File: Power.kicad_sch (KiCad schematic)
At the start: 0 parts

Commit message: [#81782] Add DC section
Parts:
- added C17: C_1u_25V_0402, antmicro-footprints:C_0402_1005Metric, symbol antmicroCapacitors0402:C_1u_25V_0402
- added C18, C23, C24, C25, C30, C31: C_100n_0402, antmicro-footprints:C_0402_1005Metric, symbol antmicroCapacitors0402:C_100n_0402
- added C19, C20, C21, C22: C_22u_25V_0805, antmicro-footprints:C_0805_2012Metric, symbol antmicroCapacitorsmisc:C_22u_25V_0805
- added C26, C27: C_1u_0402, antmicro-footprints:C_0402_1005Metric, symbol antmicroCapacitors0402:C_1u_0402
- added C28, C29: C_4u7_25V_0402, antmicro-footprints:C_0402_1005Metric, symbol antmicroCapacitors0402:C_4u7_25V_0402
- added C32, C33, C34, C35, C36, C37, C38, C39: C_22u_16V_0603, antmicro-footprints:C_0603_1608Metric_EIA, symbol antmicroCapacitors0603:C_22u_16V_0603
- added D1, D3: DF2S30FS_SOD, antmicro-footprints:SOD-923, symbol antmicroTVSDiodes:DF2S30FS_SOD
- added D2: LED_G_0603_LTST-C190GKT, antmicro-footprints:LED_0603_1608Metric_G, symbol antmicroLEDIndicationDiscrete:LED_G_0603_LTST-C190GKT
- added D4, D5: ESD9X5.0ST5G, antmicro-footprints:SOD-923, symbol antmicroTVSDiodes:ESD9X5.0ST5G
- added J2: Molex_Nano-Fit_1x2_SMD_1054301202, antmicro-footprints:Conn_Molex_Nano-Fit_1x2_SMD_1054301202, symbol antmicroWire2BoardConnectors:Molex_Nano-Fit_1x2_SMD_1054301202
- added L1: L_1u_20A_Bourns-SRP6050CA, antmicro-footprints:L_Bourns-SRP6050CA, symbol antmicroFixedInductors:L_1u_20A_Bourns-SRP6050CA
- added L2: L_560n_17.7A_Bourns-SRP5030CA, antmicro-footprints:L_Bourns-SRP5030CA, symbol antmicroFixedInductors:L_560n_17.7A_Bourns-SRP5030CA
- added Q1, Q3, Q5: SSM3J332R, antmicro-footprints:SOT-23-3, symbol antmicroTransistorsFETsMOSFETsSingle:SSM3J332R
- added Q2: BCM857BS-7-F, antmicro-footprints:SOT-363, symbol antmicroTransistorsBipolarArrays:BCM857BS-7-F
- added Q4: PJE138K, antmicro-footprints:SOT-523, symbol antmicroTransistorsFETsMOSFETsSingle:PJE138K
- added R10, R11, R12, R15, R16, R9: R_499k_0402, antmicro-footprints:R_0402_1005Metric, symbol antmicroResistors0402:R_499k_0402
- added R13: R_20k_0402, antmicro-footprints:R_0402_1005Metric, symbol antmicroResistors0402:R_20k_0402
- added R14: R_2k7_0402, antmicro-footprints:R_0402_1005Metric, symbol antmicroResistors0402:R_2k7_0402
- added R17: R_0R_0402, antmicro-footprints:R_0402_1005Metric, symbol antmicroResistors0402:R_0R_0402
- added R18: R_73k2_0402, antmicro-footprints:R_0402_1005Metric, symbol antmicroResistors0402:R_73k2_0402
- added R19, R21, R24, R3, R4, R8: R_10k_0402, antmicro-footprints:R_0402_1005Metric, symbol antmicroResistors0402:R_10k_0402
- added R20: R_45k3_0402, antmicro-footprints:R_0402_1005Metric, symbol antmicroResistors0402:R_45k3_0402
- added R22, R23, R25, R6: R_0R_22.4A_0603, antmicro-footprints:R_0603_1608Metric, symbol antmicroResistors0603:R_0R_22.4A_0603
- added R5, R7: R_4k7_0402, antmicro-footprints:R_0402_1005Metric, symbol antmicroResistors0402:R_4k7_0402
- added TP1, TP2, TP3, TP4: TP_0.75mm_SMD, antmicro-footprints:TP_SMD_0.75mm, symbol antmicroTestPoints:TP_0.75mm_SMD
- added U1, U2: SIC431AED-T1-GE3, antmicro-footprints:MLP44-24L_4x4x0.75mm, symbol antmicroDCDCConverters:SIC431AED-T1-GE3
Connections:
- new net: D1.1 (C), J2.1, Q1.3 (D), Q2.4
- new net: C17.1, C18.1, Q3.1 (G), R5.1, R7.2
- new net: D2.2 (A), R8.1
- new net: Q1.1 (G), Q2.6, R4.2
- new net: Q2.2, Q2.3, Q2.5, R3.2
- new net: U1.10 (GL), U1.11 (GL), U1.28 (GL)
- new net: U2.10 (GL), U2.11 (GL), U2.28 (GL)
- new net +3V3: D5.1 (C), R23.2, TP3.1
- new net +5V: Q5.3 (D), R25.2, TP4.1
- new net +5V_SoM: D4.1 (C), Q5.2 (S), R22.2, R24.2, R25.1
- new net 3V3_BOOT: C31.2, U2.23 (BOOT)
- new net 3V3_EN: R17.2, U2.19 (EN)
- new net 3V3_FB: R20.1, R21.2, U2.17 (FB)
- new net 3V3_MODE1: R11.1, R12.2, U2.21 (MODE1)
- new net 3V3_MODE2: R16.2, U2.20 (MODE2)
- new net 3V3_OUT: C33.2, C35.2, C37.2, C39.2, L2.2, R20.2, R23.1, U2.18 (V_{OUT})
- new net 3V3_PHASE: C31.1, U2.24 (PHASE)
- new net 3V3_SW: L2.1, U2.5 (SW), U2.6 (SW), U2.7 (SW), U2.8 (SW), U2.9 (SW)
- new net 3V3_VDD: C27.2, R11.2, U2.15 (V_{DD})
- new net 3V3_VDRV: C29.2, U2.12 (V_{DRV})
- new net 5V_BOOT: C30.2, U1.23 (BOOT)
- new net 5V_EN: C25.1, R13.1, R14.2, U1.19 (EN)
- new net 5V_FB: R18.1, R19.2, U1.17 (FB)
- new net 5V_GATE: Q4.3 (D), Q5.1 (G), R24.1
- new net 5V_MODE1: R10.2, R9.1, U1.21 (MODE1)
- new net 5V_MODE2: R15.2, U1.20 (MODE2)
- new net 5V_OUT: C32.2, C34.2, C36.2, C38.2, L1.2, R18.2, R22.1, U1.18 (V_{OUT})
- new net 5V_PHASE: C30.1, U1.24 (PHASE)
- new net 5V_SW: L1.1, U1.5 (SW), U1.6 (SW), U1.7 (SW), U1.8 (SW), U1.9 (SW)
- new net 5V_VDD: C26.2, R9.2, U1.15 (V_{DD})
- new net 5V_VDRV: C28.2, U1.12 (V_{DRV})
- new net GND: C19.1, C20.1, C21.1, C22.1, C23.2, C24.2, C25.2, C26.1, C27.1, C28.1, C29.1, C32.1, C33.1, C34.1, C35.1, C36.1, C37.1, C38.1, C39.1, D1.2 (A), D2.1 (C), D3.2 (A), D4.2 (A), D5.2 (A), J2.2, J2.MP, Q4.2 (S), R10.1, R12.1, R14.1, R15.1, R16.1, R19.1, R21.1, R3.1, R4.1, R7.1, TP2.1, U1.13 (P_{GND}), U1.16 (A_{GND}), U1.25 (A_{GND}), U1.27 (P_{GND}), U1.3 (P_{GND}), U1.4 (P_{GND}), U2.13 (P_{GND}), U2.16 (A_{GND}), U2.25 (A_{GND}), U2.27 (P_{GND}), U2.3 (P_{GND}), U2.4 (P_{GND})
- new net VCC: C18.2, C19.2, C20.2, C21.2, C22.2, C23.1, C24.1, D3.1 (C), Q3.3 (D), R13.2, R6.2, R8.2, TP1.1, U1.1 (V_{IN}), U1.2 (V_{IN}), U1.22 (V_{IN}), U1.26 (V_{IN}), U2.1 (V_{IN}), U2.2 (V_{IN}), U2.22 (V_{IN}), U2.26 (V_{IN})
- new net VCC_IN: C17.2, Q1.2 (S), Q2.1, Q3.2 (S), R5.2, R6.1
- new net ~{RESET}: Q4.1 (G), R17.1
- no-connect marks 0 -> 4
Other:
- added sheet PoE (PoE.kicad_sch)
- added sheet Usb_pd (Usb_pd.kicad_sch)
- note added: "3V3 @12A"
- note added: "5V @12A"
- note added: "9 - 20 V"
- note added: "R_{FB_H} = (R_{FB_L}(V_{OUT}-0.6))/0.6"
- note added: "Sets UVLO to 8.4V"
- note added: "V_{OUT} = 0.6*(45k3+10k)/10k = 3.318[V]"
- note added: "V_{OUT} = 0.6*(R_{FB_H}+R_{FB_L})/R_{FB_L}"

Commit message: [#81782] Add PoE
[#81782] Rename sheets, change ideal diode circuit, add ULS-12/8.3

[#81782] Remove DC.kicad_sch

[#81782] change Q3
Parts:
- removed Q1, Q3: SSM3J332R, antmicro-footprints:SOT-23-3, symbol antmicroTransistorsFETsMOSFETsSingle:SSM3J332R
- removed Q2: BCM857BS-7-F, antmicro-footprints:SOT-363, symbol antmicroTransistorsBipolarArrays:BCM857BS-7-F
- removed R3, R4: R_10k_0402, antmicro-footprints:R_0402_1005Metric, symbol antmicroResistors0402:R_10k_0402
- added C17, C65: C_100n_50V_X8L_0402, antmicro-footprints:C_0402_1005Metric, symbol antmicroCapacitors0402:C_100n_50V_X8L_0402
- added C18, C66: C_1u_25V_0402, antmicro-footprints:C_0402_1005Metric, symbol antmicroCapacitors0402:C_1u_25V_0402
- added D2: DF2S30FS_SOD, antmicro-footprints:SOD-923, symbol antmicroTVSDiodes:DF2S30FS_SOD
- added Q1, Q2: SQS401EN-T1_BE3, antmicro-footprints:Vishay_PowerPAK_1212-8_Single, symbol antmicroTransistorsFETsMOSFETsSingle:SQS401EN-T1_BE3
- added Q4: SI7613DN-T1-GE3, antmicro-footprints:Vishay_PowerPAK_1212-8_Single, symbol antmicroTransistorsFETsMOSFETsSingle:SI7613DN-T1-GE3
- added U1, U11: LTC4412IS6, antmicro-footprints:SOT-23-6, symbol antmicroPMICORControllersIdealDiodes:LTC4412IS6
- renumbered C17 to C19, C18 to C20, C19 to C21, C20 to C22, C21 to C23, C22 to C24, C23 to C25, C24 to C26, C25 to C27, C26 to C28, C27 to C29, C28 to C30, C29 to C31, C30 to C32, C31 to C33, C32 to C34, C33 to C35, C34 to C36, C35 to C37, C36 to C38, C37 to C39, C38 to C40, C39 to C41, D2 to D3, D3 to D4, D4 to D5, D5 to D6, Q4 to Q5, Q5 to Q6, U1 to U2, U2 to U3
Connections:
- net GND: now also C17.1, C18.1, C65.1, C66.1, D2.2 (A), U1.2 (GND), U1.3 (CTL), U11.2 (GND), U11.3 (CTL)
- net VCC: now also Q4.1 (S), Q4.2 (S), Q4.3 (S)
- net at D1.1 (C), J2.1: now also C17.2, Q1.5 (D), U1.1 (IN)
- net at C19.1, C20.1, R5.1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: now also Q4.4 (G)
- net VCC_IN renamed USBPD0_HV
- net USBPD0_HV: now also C18.2, C66.2, Q1.1 (S), Q1.2 (S), Q1.3 (S), Q2.1 (S), Q2.2 (S), Q2.3 (S), Q4.5 (D), U1.6 (SENSE), U11.6 (SENSE)
- new net: Q2.4 (G), U11.5 (GATE)
- new net: Q1.4 (G), U1.5 (GATE)
- new net POE: C65.2, D2.1 (C), Q2.5 (D), U11.1 (IN)
- no-connect marks 4 -> 6
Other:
- removed sheet PoE
- removed sheet Usb_pd
- moved on the sheet: C19, C20, D1, D3, D4, J2, R5, R6, R7, R8, TP1, TP2

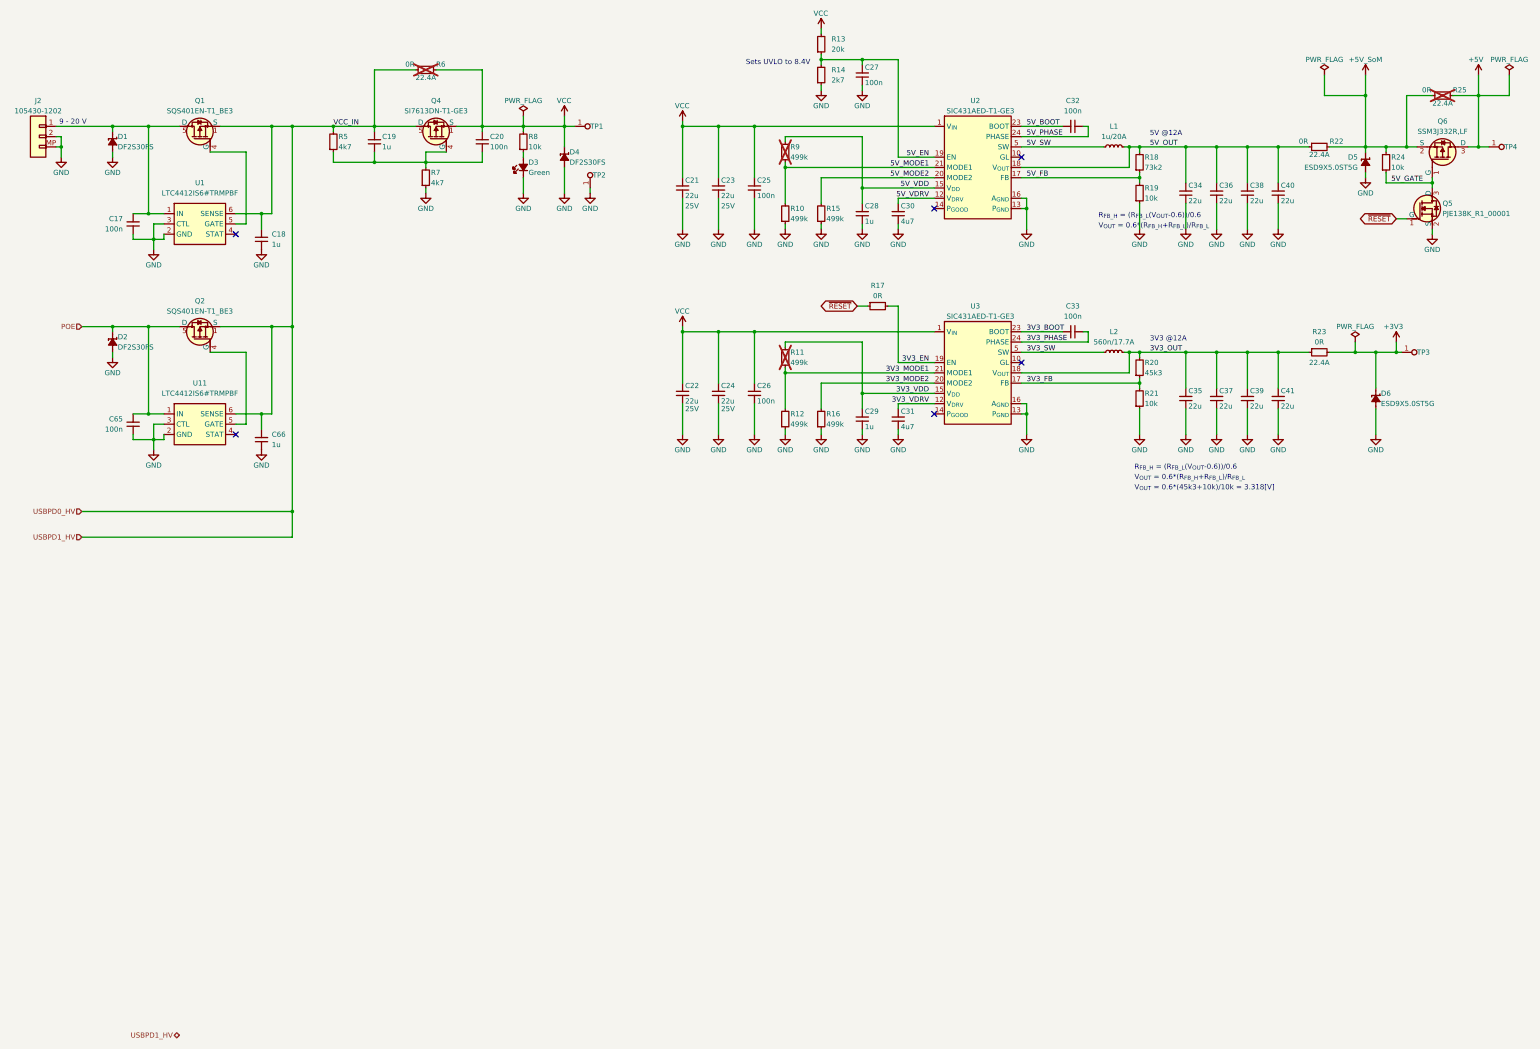
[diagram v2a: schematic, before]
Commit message: [#81970] Add 12V DC-DC
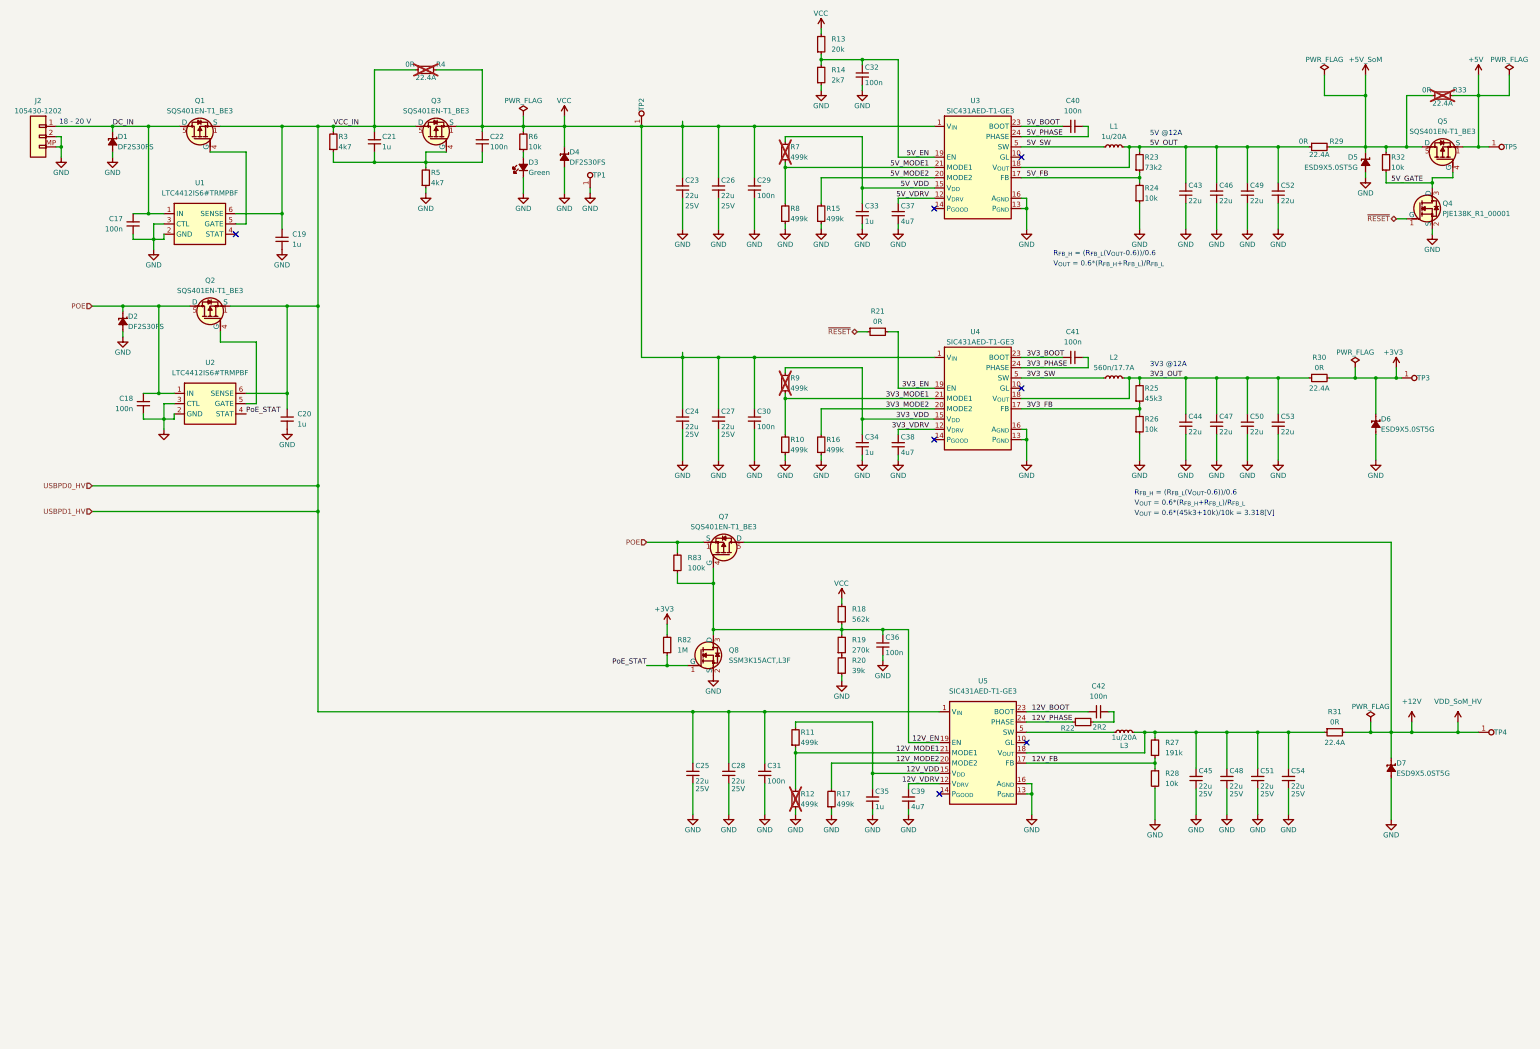
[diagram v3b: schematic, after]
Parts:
- removed Q4: SI7613DN-T1-GE3, antmicro-footprints:Vishay_PowerPAK_1212-8_Single, symbol antmicroTransistorsFETsMOSFETsSingle:SI7613DN-T1-GE3
- removed Q6: SSM3J332R, antmicro-footprints:SOT-23-3, symbol antmicroTransistorsFETsMOSFETsSingle:SSM3J332R
- added C25, C28, C45, C48, C51, C54: C_22u_25V_0805, antmicro-footprints:C_0805_2012Metric, symbol antmicroCapacitorsmisc:C_22u_25V_0805
- added C31, C36: C_100n_0402, antmicro-footprints:C_0402_1005Metric, symbol antmicroCapacitors0402:C_100n_0402
- added C35: C_1u_0402, antmicro-footprints:C_0402_1005Metric, symbol antmicroCapacitors0402:C_1u_0402
- added C39: C_4u7_25V_0402, antmicro-footprints:C_0402_1005Metric, symbol antmicroCapacitors0402:C_4u7_25V_0402
- added C42: C_100n_16V_X7R_0402, antmicro-footprints:C_0402_1005Metric, symbol antmicroCapacitors0402:C_100n_16V_X7R_0402
- added D7: ESD9X5.0ST5G, antmicro-footprints:SOD-923, symbol antmicroTVSDiodes:ESD9X5.0ST5G
- added L3: L_1u_20A_Bourns-SRP6050CA, antmicro-footprints:L_Bourns-SRP6050CA, symbol antmicroFixedInductors:L_1u_20A_Bourns-SRP6050CA
- added Q3, Q5, Q7: SQS401EN-T1_BE3, antmicro-footprints:Vishay_PowerPAK_1212-8_Single, symbol antmicroTransistorsFETsMOSFETsSingle:SQS401EN-T1_BE3
- added Q8: SSM3K15ACT, antmicro-footprints:CST3-3, symbol antmicroTransistorsFETsMOSFETsSingle:SSM3K15ACT
- added R11, R12, R17: R_499k_0402, antmicro-footprints:R_0402_1005Metric, symbol antmicroResistors0402:R_499k_0402
- added R18: R_562k_0402, antmicro-footprints:R_0402_1005Metric, symbol antmicroResistors0402:R_562k_0402
- added R19: R_270k_0402, antmicro-footprints:R_0402_1005Metric, symbol antmicroResistors0402:R_270k_0402
- added R20: R_39k_0402, antmicro-footprints:R_0402_1005Metric, symbol antmicroResistors0402:R_39k_0402
- added R22: R_2R2_0402, antmicro-footprints:R_0402_1005Metric, symbol antmicroResistors0402:R_2R2_0402
- added R27: R_191k_0402, antmicro-footprints:R_0402_1005Metric, symbol antmicroResistors0402:R_191k_0402
- added R28: R_10k_0402, antmicro-footprints:R_0402_1005Metric, symbol antmicroResistors0402:R_10k_0402
- added R31: R_0R_22.4A_0603, antmicro-footprints:R_0603_1608Metric, symbol antmicroResistors0603:R_0R_22.4A_0603
- added R82: R_1M_0402, antmicro-footprints:R_0402_1005Metric, symbol antmicroResistors0402:R_1M_0402
- added R83: R_100k_0201, antmicro-footprints:R_0201, symbol antmicroResistorsmisc:R_100k_0201
- added TP4: TP_0.75mm_SMD, antmicro-footprints:TP_SMD_0.75mm, symbol antmicroTestPoints:TP_0.75mm_SMD
- added U5: SIC431AED-T1-GE3, antmicro-footprints:MLP44-24L_4x4x0.75mm, symbol antmicroDCDCConverters:SIC431AED-T1-GE3
- renumbered C65 to C18, C18 to C19, C66 to C20, C19 to C21, C20 to C22, C21 to C23, C22 to C24, C23 to C26, C24 to C27, C25 to C29, C26 to C30, C27 to C32, C28 to C33, C29 to C34, C30 to C37, C31 to C38, C32 to C40, C33 to C41, C34 to C43, C35 to C44, C36 to C46, C37 to C47, C38 to C49, C39 to C50, C40 to C52, C41 to C53, Q5 to Q4, R12 to R10, R17 to R21, R18 to R23, R19 to R24, R20 to R25, R21 to R26, R22 to R29, R5 to R3, R23 to R30, R24 to R32, R25 to R33, R6 to R4, R7 to R5, R8 to R6, R9 to R7, R10 to R8, R11 to R9, TP2 to TP1, TP1 to TP2, TP4 to TP5, U11 to U2, U2 to U3, U3 to U4
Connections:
- net +3V3: now also R82.2
- net +5V: now also Q5.1 (S), Q5.2 (S), Q5.3 (S)
- net +5V_SoM: now also Q5.5 (D)
- net 5V_GATE: now also Q5.4 (G)
- net GND: now also C25.1, C28.1, C31.2, C35.1, C36.2, C39.1, C45.1, C48.1, C51.1, C54.1, D7.2 (A), Q8.2 (S), R12.1, R17.1, R20.1, R28.2, U5.13 (P_{GND}), U5.16 (A_{GND}), U5.25 (A_{GND}), U5.27 (P_{GND}), U5.3 (P_{GND}), U5.4 (P_{GND})
- net POE: now also Q7.1 (S), Q7.2 (S), Q7.3 (S), R83.2
- net USBPD0_HV: now also C25.2, C28.2, C31.1, Q3.5 (D), U5.1 (V_{IN}), U5.2 (V_{IN}), U5.22 (V_{IN}), U5.26 (V_{IN})
- net VCC: now also Q3.1 (S), Q3.2 (S), Q3.3 (S), R18.2
- net DC_IN: now reaches C17.2, D1.1 (C), J2.1, Q1.5 (D), U1.1 (IN)
- net at C21.1, C22.1, R3.1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: now also Q3.4 (G)
- net PoE_STAT: now reaches U2.4 (STAT)
- net PoE_STAT: now also Q8.1 (G), R82.1
- new net: C45.2, C48.2, C51.2, C54.2, L3.2, R27.2, R31.1, U5.18 (V_{OUT})
- new net: L3.1, U5.5 (SW), U5.6 (SW), U5.7 (SW), U5.8 (SW), U5.9 (SW)
- new net: R19.1, R20.2
- new net: U5.10 (GL), U5.11 (GL), U5.28 (GL)
- new net: C42.1, R22.2
- new net +12V: D7.1 (C), Q7.5 (D), R31.2, TP4.1
- new net 12V_BOOT: C42.2, U5.23 (BOOT)
- new net 12V_EN: C36.1, Q7.4 (G), Q8.3 (D), R18.1, R19.2, R83.1, U5.19 (EN)
- new net 12V_FB: R27.1, R28.1, U5.17 (FB)
- new net 12V_MODE1: R11.1, R12.2, U5.21 (MODE1)
- new net 12V_MODE2: R17.2, U5.20 (MODE2)
- new net 12V_PHASE: R22.1, U5.24 (PHASE)
- new net 12V_VDD: C35.2, R11.2, U5.15 (V_{DD})
- new net 12V_VDRV: C39.2, U5.12 (V_{DRV})
- no-connect marks 6 -> 7
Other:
- note added: "18 - 20 V"
- note removed: "9 - 20 V"
- note removed: "Sets UVLO to 8.4V"
- moved on the sheet: C18, C19, C20, C24, C27, C30, C34, C38, C41, C44, C47, C50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
